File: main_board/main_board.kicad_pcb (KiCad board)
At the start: 2 copper layers, 160 x 110 mm, 152 parts, among them IC1 MP2722GRH-0000-Z, IC2 MP3429GL-Z, IC4 TS921ID, IC5 CY7C65632-28LTXC, IC6 TS921ID, J1 USB3_A, J10 Conn_01x22_Female, J11 501568-0607-TR325, J12 SM04B-XSRS-ETBLFSN, J13 SM10B-XSRS-ETB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

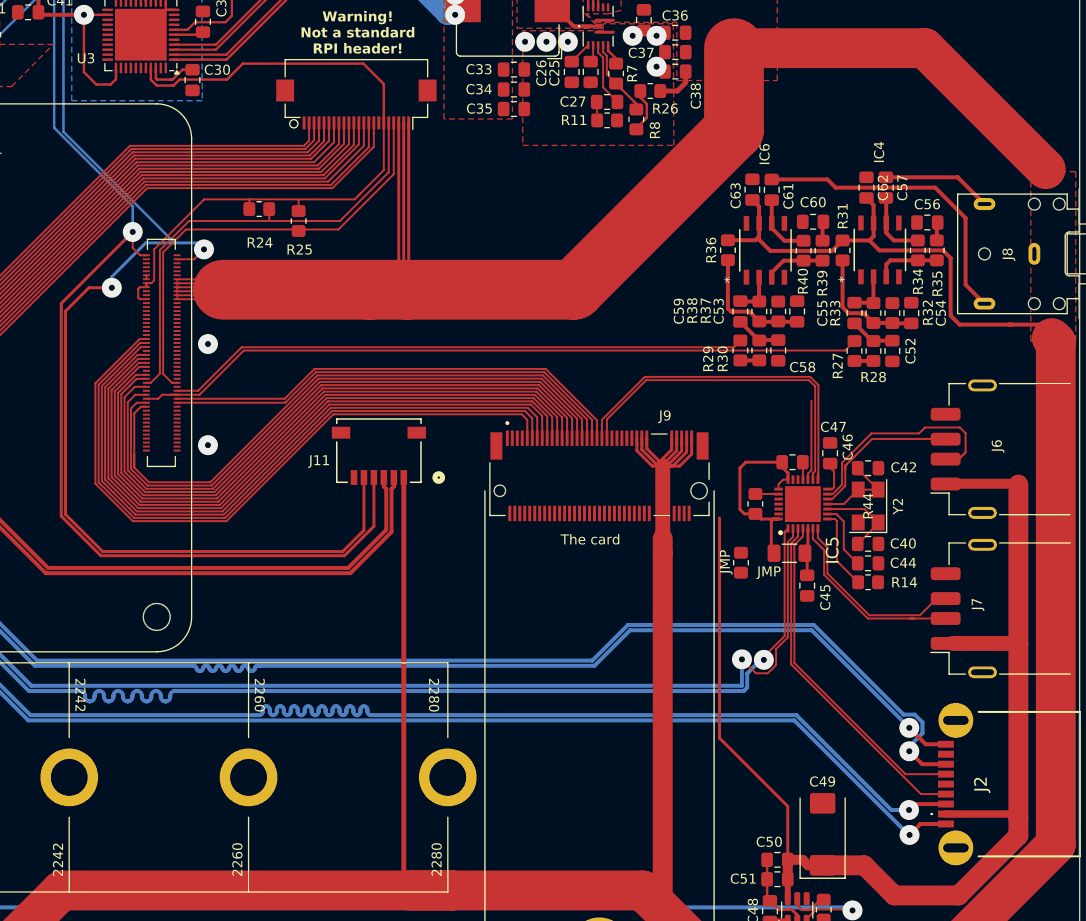
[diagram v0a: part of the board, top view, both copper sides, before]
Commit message: Cleanup, improve ground situation
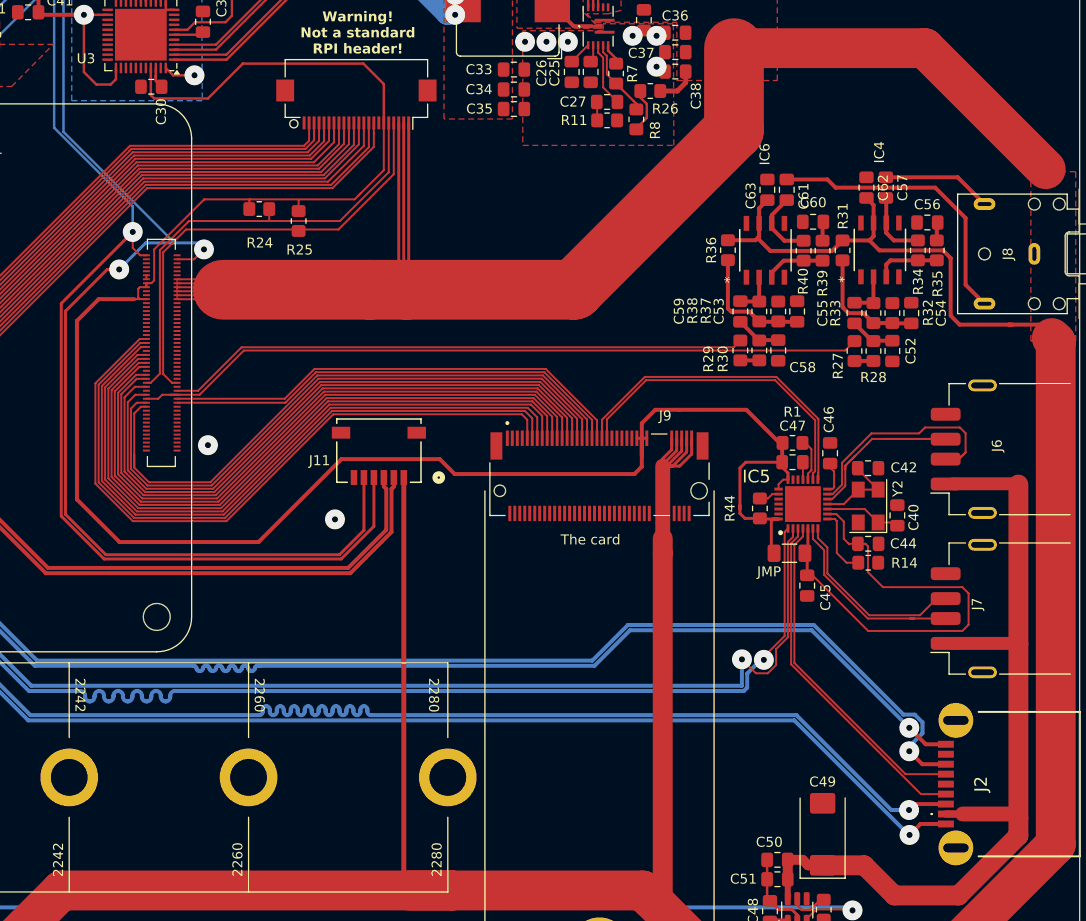
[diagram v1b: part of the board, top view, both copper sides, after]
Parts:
- removed the JMP at (153.9, 87.8)
- added R1: 10K, Resistor_SMD:R_0805_2012Metric_Pad1.20x1.40mm_HandSolder, F.Cu at (159.1, 75.7)
- moved C30 4.19 mm to (94.7, 40.0), turned to 0 degrees
- moved C40 4.10 mm to (169.6, 83.0), turned to 90 degrees
- moved C44 1.96 mm to (166.7, 85.8)
- moved R14 1.96 mm to (166.7, 87.8)
- moved C61 1.51 mm to (158.5, 50.3)
- moved C63 1.50 mm to (156.6, 50.3)
- moved R44 0.64 mm to (155.8, 82.3)
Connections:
- C44 pad 1: /USB hub/HUB3V3 -> /CM5_GPIO/+3.3v
- C45 pad 1: /USB hub/HUB3V3 -> /CM5_GPIO/+3.3v
- C47 pad 1: /USB hub/HUB3V3 -> /CM5_GPIO/+3.3v
- IC5 pad 17: /USB hub/HUB3V3 -> Net-(IC5-RESET#)
- IC5 pad 21: /USB hub/HUB3V3 -> /CM5_GPIO/+3.3v
- IC5 pad 22: /USB hub/HUB3V3 -> /CM5_GPIO/+3.3v
- IC5 pad 27: /USB hub/VBUS -> unconnected-(IC5-VCC-Pad27)
- IC5 pad 28: /USB hub/HUB3V3 -> /CM5_GPIO/+3.3v
- IC5 pad 5: /USB hub/HUB3V3 -> /CM5_GPIO/+3.3v
- IC5 pad 9: /USB hub/HUB3V3 -> /CM5_GPIO/+3.3v
- J9 pad 53: /Battery management/+5V -> /CM5_GPIO/+3.3v
- J9 pad 55: /Battery management/+5V -> /CM5_GPIO/+3.3v
- J9 pad 57: /Battery management/+5V -> /CM5_GPIO/+3.3v
- JMP pad 1: /USB hub/HUB3V3 -> /CM5_GPIO/+3.3v
- JMP pad 2: Net-(IC5-SELFPWR) -> /CM5_GPIO/+3.3v
- R44 pad 1: /USB hub/HUB3V3 -> /CM5_GPIO/+3.3v
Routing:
- net /CM5_GPIO/+3.3v: track 71.1 -> 255.9 mm
- net /USB hub/VBUS: track 124.2 -> 87.0 mm
- net /USB hub/HUB3V3: track 35.5 -> 0.00 mm
- net /Battery management/+5V: track 698.5 -> 687.3 mm
- net Net-(IC5-SELFPWR): track 6.58 -> 0.00 mm
- net Net-(IC5-RESET#): track 0.00 -> 4.37 mm
- net /Battery management/PMIC_3.3V: track 60.7 -> 63.9 mm, vias 2 -> 3
- net Net-(U3-AREF): track 5.18 -> 2.40 mm
- net /The card/USB2_2_DP: track 34.1 -> 32.1 mm
- net /The card/USB2_2_DN: track 35.9 -> 33.9 mm
- net Net-(C61-Pad1): track 30.4 -> 28.9 mm
- net Net-(IC5-RREF): track 8.07 -> 6.80 mm
- net Net-(IC5-XIN): track 8.66 -> 7.82 mm
- net Net-(IC6-OUTPUT): track 6.53 -> 7.16 mm

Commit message: More ground improvements
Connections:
- J9 pad 43: GND -> /CM5_GPIO/+3.3v
- J9 pad 45: GND -> /CM5_GPIO/+3.3v
- J9 pad 47: GND -> /CM5_GPIO/+3.3v
- J9 pad 53: /CM5_GPIO/+3.3v -> GND
- J9 pad 55: /CM5_GPIO/+3.3v -> GND
- J9 pad 57: /CM5_GPIO/+3.3v -> GND
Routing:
- net /CM5_GPIO/+3.3v: track 255.9 -> 255.1 mm
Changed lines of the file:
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@@
 			(size 0.3 1.55)
 			(layers "F.Cu" "F.Paste" "F.Mask")
-			(net 1 "GND")
+			(net 26 "/CM5_GPIO/+3.3v")
 			(pintype "bidirectional")
 			(solder_mask_margin 0.102)
@@
 			(size 0.3 1.55)
 			(layers "F.Cu" "F.Paste" "F.Mask")
-			(net 1 "GND")
+			(net 26 "/CM5_GPIO/+3.3v")
 			(pintype "bidirectional")
 			(solder_mask_margin 0.102)
@@
 			(size 0.3 1.55)
 			(layers "F.Cu" "F.Paste" "F.Mask")
-			(net 1 "GND")
+			(net 26 "/CM5_GPIO/+3.3v")
 			(pintype "bidirectional")
 			(solder_mask_margin 0.102)
@@
 			(size 0.3 1.55)
 			(layers "F.Cu" "F.Paste" "F.Mask")
-			(net 26 "/CM5_GPIO/+3.3v")
+			(net 1 "GND")
 			(pintype "bidirectional")
 			(solder_mask_margin 0.102)
@@
 			(size 0.3 1.55)
 			(layers "F.Cu" "F.Paste" "F.Mask")
-			(net 26 "/CM5_GPIO/+3.3v")
+			(net 1 "GND")
 			(pintype "bidirectional")
 			(solder_mask_margin 0.102)
@@
 			(size 0.3 1.55)
 			(layers "F.Cu" "F.Paste" "F.Mask")
-			(net 26 "/CM5_GPIO/+3.3v")
+			(net 1 "GND")
 			(pintype "bidirectional")
 			(solder_mask_margin 0.102)
@@
 	)
 	(segment
-		(start 143.45 75.255)
-		(end 144.45 75.255)
-		(width 0.3)
-		(layer "F.Cu")
-		(net 26)
-	)
-	(segment
-		(start 143.95 75.255)
-		(end 143.95 78.1)
-		(width 0.4)
-		(layer "F.Cu")
-		(net 26)
-	)
-	(segment
 		(start 155.8 83.3)
 		(end 154.3 83.3)
@@
 	)
 	(segment
-		(start 143.95 75.255)
-		(end 143.95 73.75)
-		(width 0.4)
-		(layer "F.Cu")
-		(net 26)
-	)
-	(segment
 		(start 157.675 80.3625)
 		(end 157.675 79.875)
@@
 	)
 	(segment
-		(start 143.2 78.85)
-		(end 125.17 78.85)
+		(start 141.45 77.75)
+		(end 141.45 75.255)
 		(width 0.4)
 		(layer "F.Cu")
@@
 	)
 	(segment
+		(start 140.95 75.255)
+		(end 141.95 75.255)
+		(width 0.3)
+		(layer "F.Cu")
+		(net 26)
+	)
+	(segment
 		(start 115.125 51.275)
 		(end 115.75 50.65)
@@
 	)
 	(segment
+		(start 145.3 72.4)
+		(end 146.3 72.4)
+		(width 0.4)
+		(layer "F.Cu")
+		(net 26)
+	)
+	(segment
 		(start 157.675 83.3625)
 		(end 157.1375 83.3625)
@@
 	)
 	(segment
+		(start 146.3 72.4)
+		(end 142.45 72.4)
+		(width 0.4)
+		(layer "F.Cu")
+		(net 26)
+	)
+	(segment
 		(start 176.125 90.2)
 		(end 176.75 90.825)
@@
 	)
 	(segment
-		(start 143.95 78.1)
-		(end 143.2 78.85)
+		(start 91.525 85.675)
+		(end 87.25 81.4)
 		(width 0.4)
 		(layer "F.Cu")
@@
 	)
 	(segment
-		(start 91.525 85.675)
-		(end 87.25 81.4)
+		(start 146.3 72.4)
+		(end 147.7 72.4)
 		(width 0.4)
 		(layer "F.Cu")
@@
 	)
 	(segment
-		(start 143.95 73.75)
-		(end 145.3 72.4)
+		(start 140.35 78.85)
+		(end 141.45 77.75)
 		(width 0.4)
 		(layer "F.Cu")
@@
 	)
 	(segment
-		(start 93.4 60.25)
-		(end 93.4 61.141)
-		(width 0.2)
+		(start 140.275 78.85)
+		(end 125.17 78.85)
+		(width 0.4)
 		(layer "F.Cu")
 		(net 26)
 	)
 	(segment
-		(start 143.95 77.05)
-		(end 143.95 75.255)
-		(width 0.4)
+		(start 93.4 60.25)
+		(end 93.4 61.141)
+		(width 0.2)
 		(layer "F.Cu")
 		(net 26)
@@
 	)
 	(segment
+		(start 142.45 72.4)
+		(end 141.45 73.4)
+		(width 0.4)
+		(layer "F.Cu")
+		(net 26)
+	)
+	(segment
 		(start 94.221 59.9)
 		(end 94.221 60.091)
@@
 	)
 	(segment
+		(start 140.275 78.85)
+		(end 140.35 78.85)
+		(width 0.4)
+		(layer "F.Cu")
+		(net 26)
+	)
+	(segment
 		(start 113.8 77.35)
 		(end 105.475 85.675)
@@
 	)
 	(segment
-		(start 145.3 72.4)
-		(end 147.7 72.4)
-		(width 0.4)
+		(start 153.8 82)
+		(end 153.8 82.4)
+		(width 0.3)
 		(layer "F.Cu")
 		(net 26)
 	)
 	(segment
-		(start 153.8 82)
-		(end 153.8 82.4)
-		(width 0.3)
+		(start 141.45 73.4)
+		(end 141.45 75.255)
+		(width 0.4)
 		(layer "F.Cu")
 		(net 26)

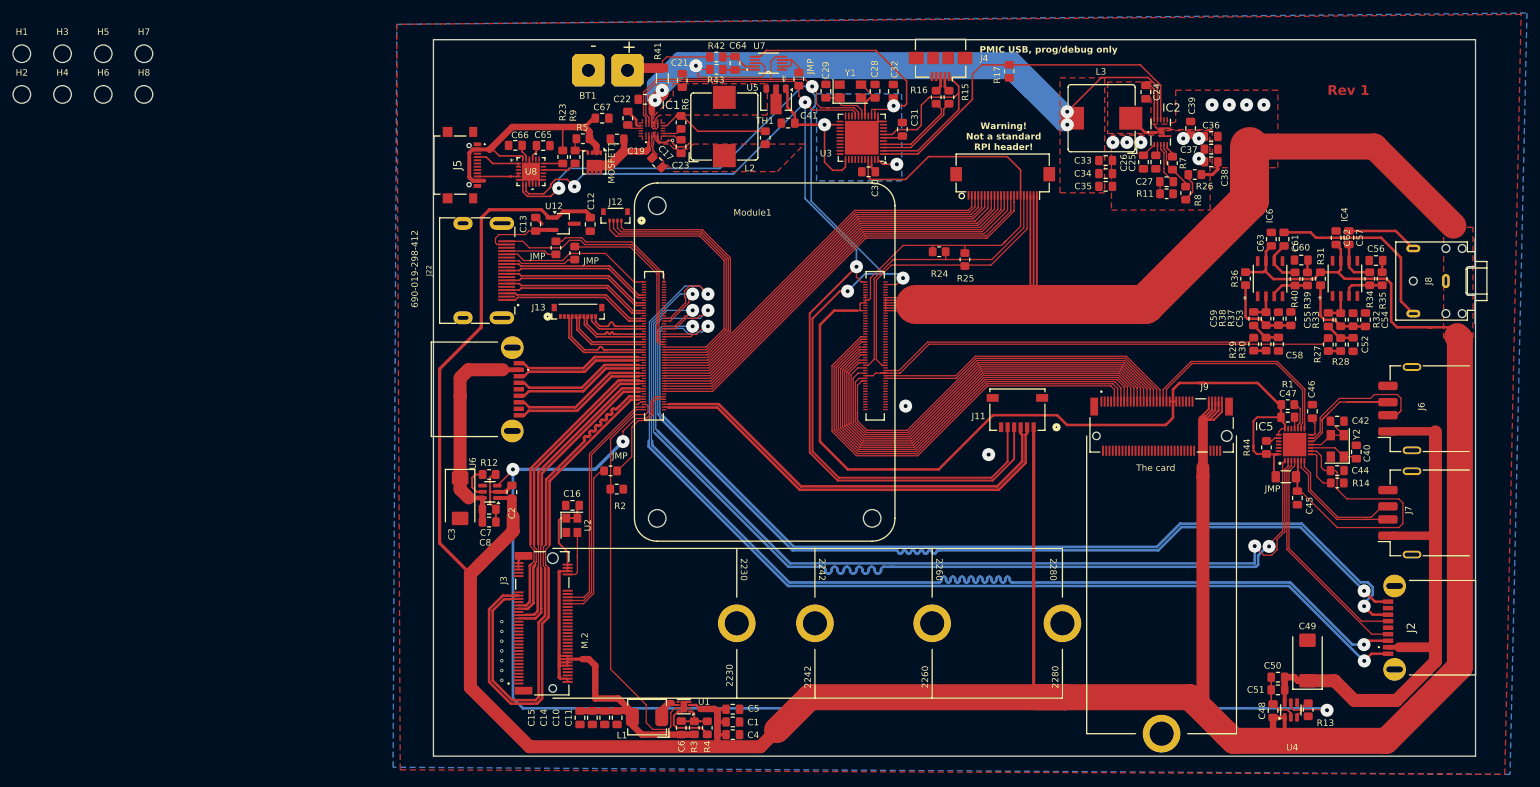
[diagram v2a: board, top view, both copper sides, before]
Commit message: Fix 32u4 high power consumption, improve QFN soldering with thick ass solder masks.
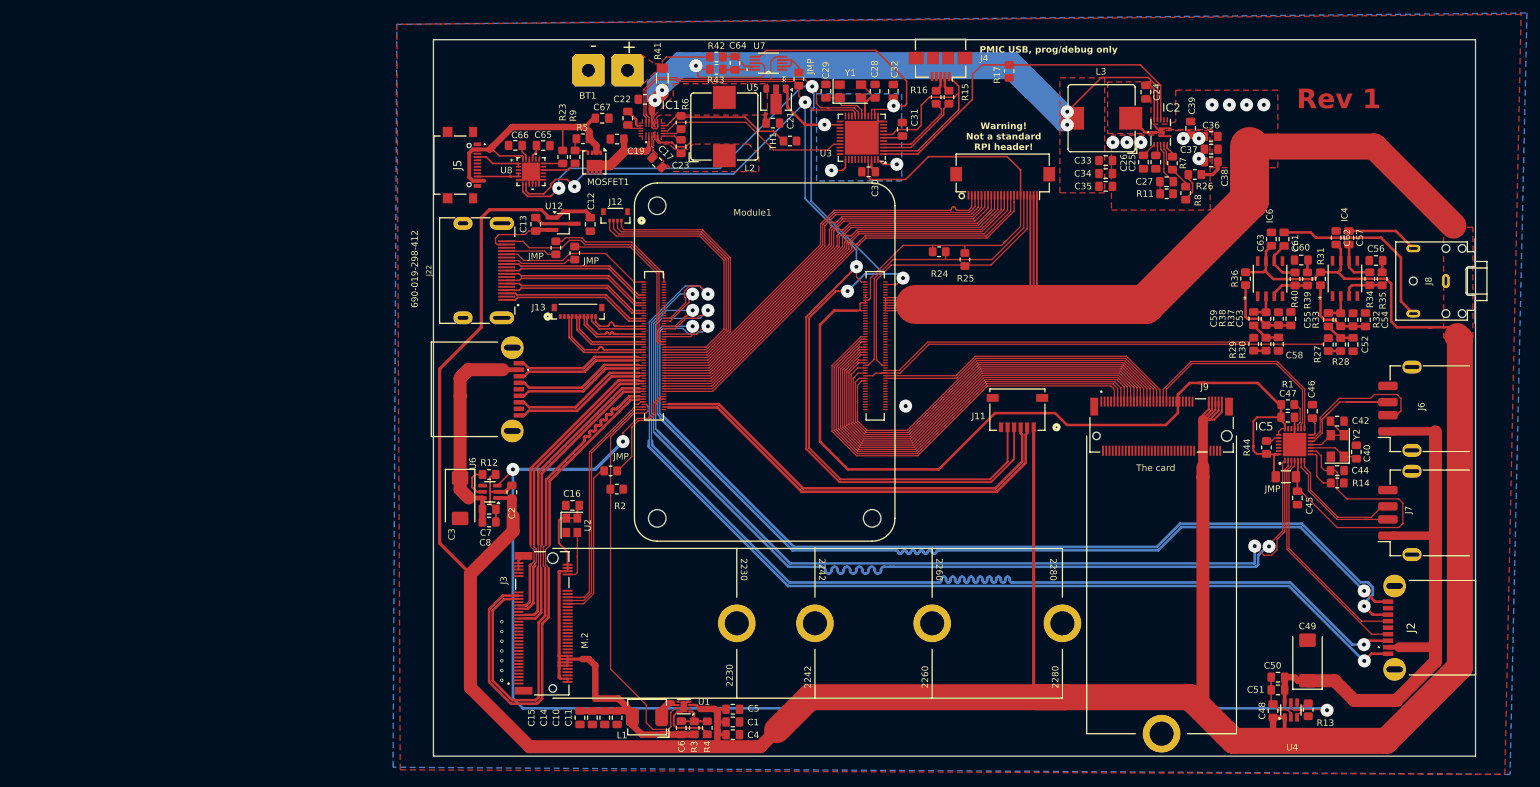
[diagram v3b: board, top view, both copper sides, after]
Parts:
- removed C41: 100n, Capacitor_SMD:C_0805_2012Metric_Pad1.18x1.45mm_HandSolder
- removed H1, H2, H3, H4, H5, H6, H7, H8: MountingHole, CM5IO:MountingHole_2.7mm_M2.5_DIN965
- C23: value 22n -> 10n
- moved C21 15.4 mm to (80.0, 32.5), turned to 0 degrees
- moved TH1 3.83 mm to (82.7, 35.2), turned to 0 degrees
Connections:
- IC1 pad 8: unconnected-(IC1-~{INT}-Pad8) -> Net-(IC1-~{INT})
- J9 pad 43: /CM5_GPIO/+3.3v -> GND
- J9 pad 45: /CM5_GPIO/+3.3v -> GND
- J9 pad 49: GND -> /CM5_GPIO/+3.3v
- U3 pad 22: GND -> unconnected-(U3-PD5-Pad22)
- U3 pad 28: unconnected-(U3-PB4-Pad28) -> GND
- U3 pad 29: unconnected-(U3-PB5-Pad29) -> GND
- U3 pad 30: unconnected-(U3-PB6-Pad30) -> Net-(IC1-~{INT})
- U3 pad 31: unconnected-(U3-PC6-Pad31) -> GND
- U3 pad 32: unconnected-(U3-PC7-Pad32) -> GND
- U3 pad 33: unconnected-(U3-~{HWB}/PE2-Pad33) -> GND
- U3 pad 8: GND -> unconnected-(U3-PB0-Pad8)
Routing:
- net Net-(IC1-~{INT}): track 0.00 -> 29.9 mm
- net GND: track 323.3 -> 334.8 mm, vias 16 -> 14
- net /Battery management/PMIC_3.3V: track 63.9 -> 55.8 mm, vias 3 -> 4
- net Net-(BT1-+): track 14.1 -> 9.11 mm
- net Net-(IC1-NTC1): track 17.4 -> 20.9 mm
- net /CM5_HighSpeed/DPHY0_D3_P: track 58.6 -> 61.0 mm
- net /CM5_HighSpeed/DPHY0_D2_P: track 60.6 -> 62.6 mm
- net /CM5_HighSpeed/DPHY0_D3_N: track 59.3 -> 61.1 mm
- net /Battery management/V_SYS: track 0.00 -> 1.55 mm
- net /CM5_HighSpeed/DPHY0_C_P: track 62.8 -> 64.3 mm
- net /CM5_HighSpeed/DPHY0_D2_N: track 61.3 -> 62.6 mm
- net /CM5_GPIO/+3.3v: track 255.1 -> 254.0 mm
- net /Battery management/IIC_SDA: track 236.3 -> 237.4 mm
- net /CM5_HighSpeed/DPHY0_D1_P: track 64.8 -> 65.9 mm
- net /CM5_HighSpeed/DPHY0_C_N: track 63.4 -> 64.4 mm
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- added copper zone on F.Cu, net Net-(BT1-+)

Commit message: Make sure, that audio jack can be hand soldered, finalize rev 1 design.
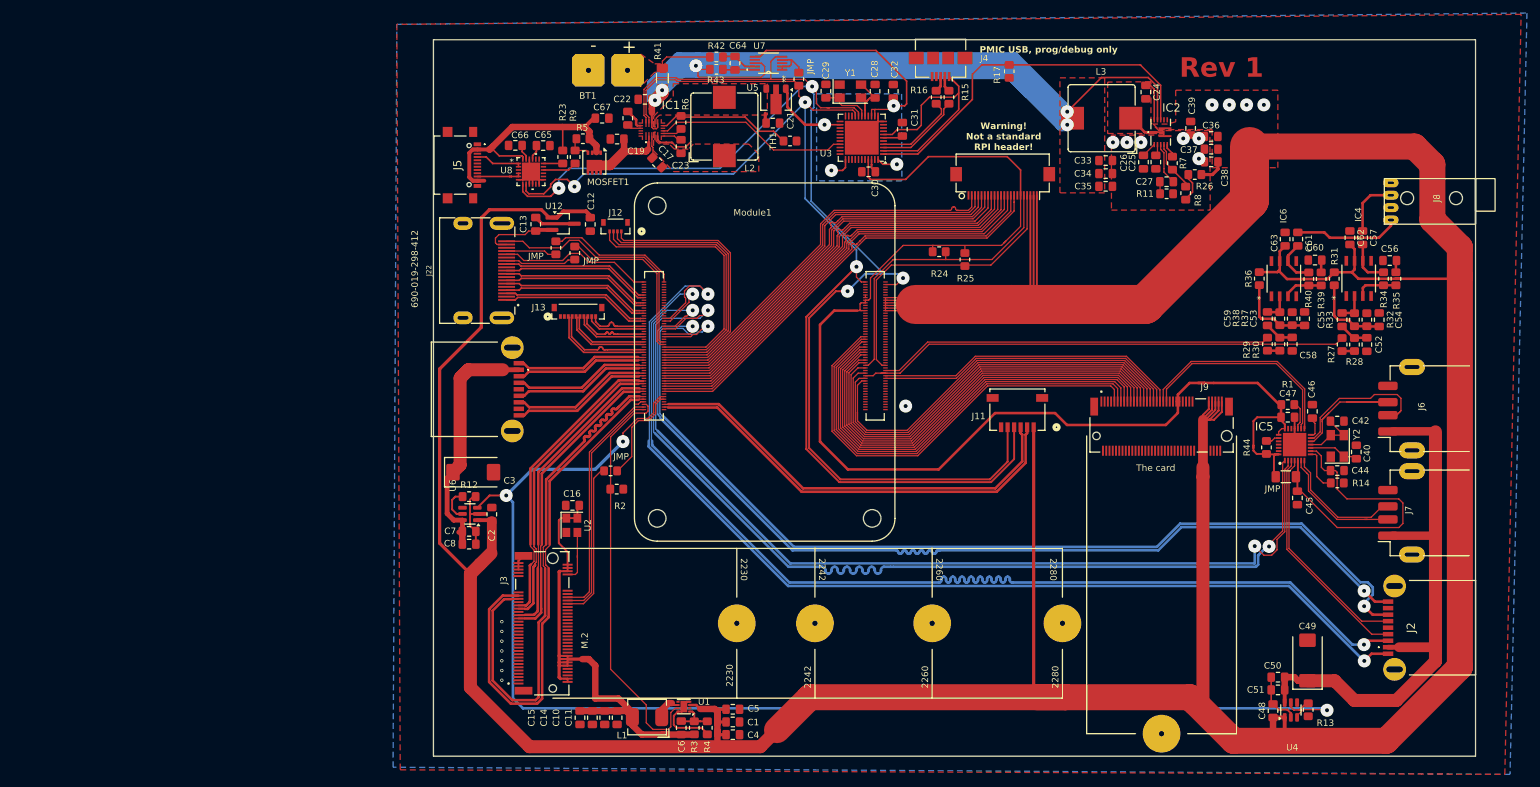
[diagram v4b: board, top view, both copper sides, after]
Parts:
- J8: footprint Connector_Audio:Jack_3.5mm_CUI_SJ1-3523N_Horizontal -> 000_custom:LUMBERG 1503 16
- moved J8 12.8 mm to (184.6, 44.0)
- moved C2 4.58 mm to (36.9, 92.6)
- moved C8 4.58 mm to (33.4, 97.2)
- moved U6 4.58 mm to (33.5, 92.5)
- moved C7 4.58 mm to (33.4, 95.2)
- moved R12 4.58 mm to (33.4, 89.8)
- moved C3 4.47 mm to (34.0, 86.1), turned to 0 degrees
- moved C52 2.11 mm to (171.2, 66.5)
- moved C53 2.11 mm to (161.7, 62.5)
- moved C54 2.11 mm to (173.1, 62.7)
- moved C57 2.11 mm to (170.6, 50.1)
- moved C59 2.11 mm to (156.0, 62.5)
- moved C61 2.11 mm to (160.6, 50.3)
- moved C62 2.11 mm to (168.6, 50.1)
- moved IC4 2.11 mm to (170.0, 56.4)
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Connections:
- J8 pad T: Net-(C57-Pad1) -> Net-(C61-Pad1)
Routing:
- net Net-(C61-Pad1): track 28.9 -> 16.3 mm
- net /Battery management/+5V: track 687.3 -> 696.9 mm
- net /CM5_HighSpeed/VBUS: track 36.1 -> 39.5 mm
- net GND: track 334.8 -> 332.2 mm
- net /CM5_GPIO/AUDIO_OUT_R: track 58.6 -> 60.7 mm
- net /CM5_GPIO/AUDIO_OUT_L: track 74.1 -> 76.2 mm
- net Net-(C57-Pad1): track 11.0 -> 9.11 mm
- net /CM5_HighSpeed/VBUS_EN: track 198.7 -> 200.1 mm
